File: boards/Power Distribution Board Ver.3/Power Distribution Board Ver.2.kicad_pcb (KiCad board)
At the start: 4 copper layers, 70 x 100 mm, 79 parts, among them J1 Screw_Terminal_01x02, J4 Screw_Terminal_01x06, U1 SIC431AED-T1-GE3, U2 SIC431AED-T1-GE3, U3 SIC431AED-T1-GE3

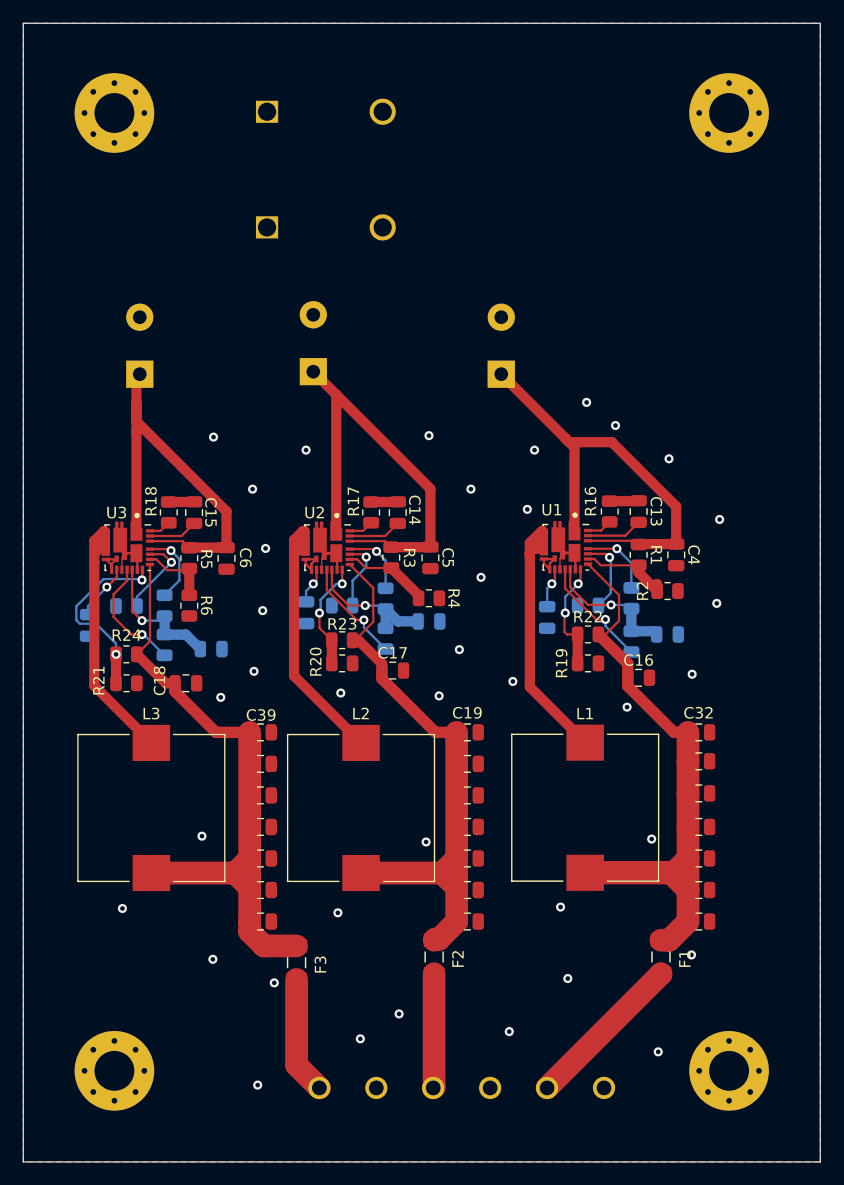
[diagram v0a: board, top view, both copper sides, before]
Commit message: GL connections and minor trace fixes
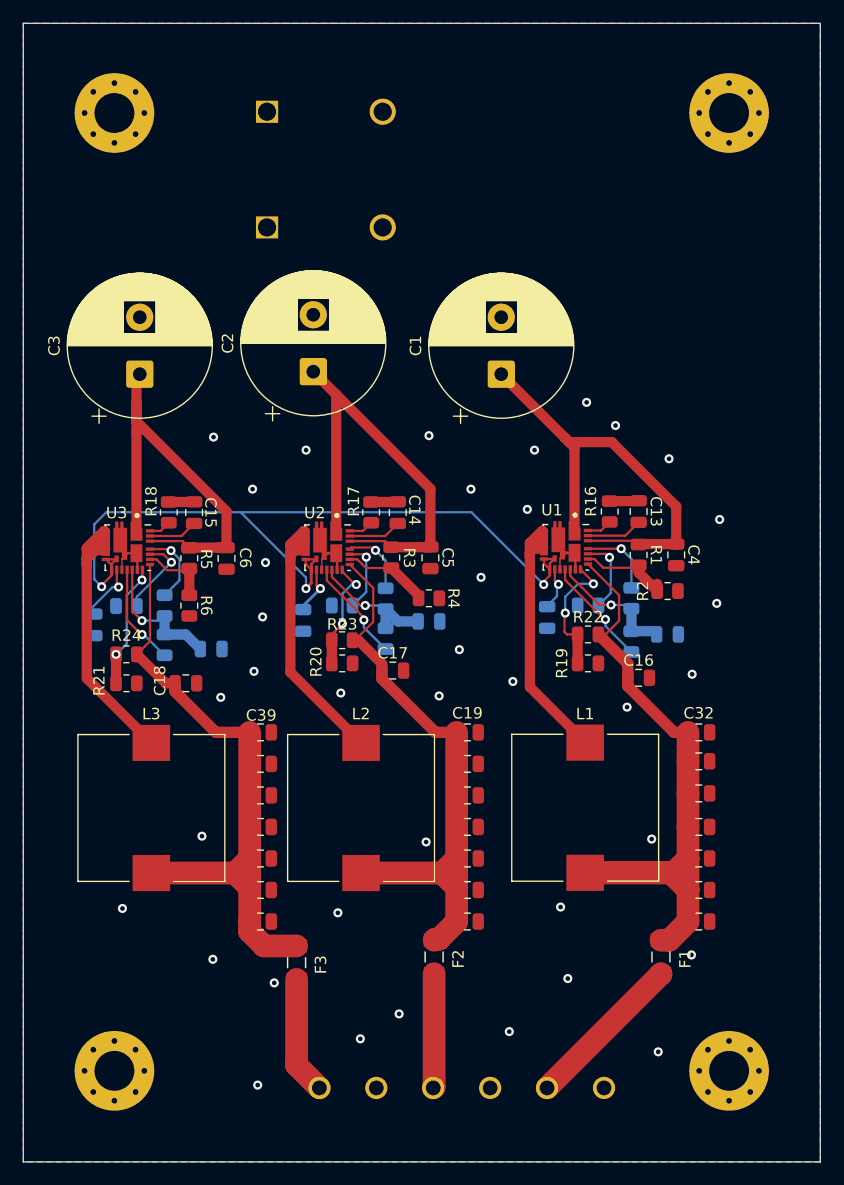
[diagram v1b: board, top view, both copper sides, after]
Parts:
- C1, C2, C3: moved to F.Cu
- L1, L2, L3: value 1uH -> 1.2uH
- R16, R17, R18: value 0 -> 3.3
- R22, R23: value 78.7k -> 73.2
- R24: value 78.7k -> 73.2k
- moved C11 0.72 mm to (42.6, 75.4)
- moved C12 0.55 mm to (24.2, 75.8)
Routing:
- net /GL: track 9.65 -> 72.3 mm, vias 0 -> 3
- net Net-(L3-Pad1): track 24.3 -> 31.8 mm
- net Net-(U3-FB): track 16.7 -> 11.0 mm
- net Net-(L2-Pad1): track 24.5 -> 29.8 mm
- net Net-(U1-FB): track 9.86 -> 11.6 mm
- net Net-(U3-PGOOD): track 10.5 -> 9.00 mm
- net Net-(U2-VDRV): track 3.21 -> 4.39 mm
- net Net-(U2-VDD): track 12.1 -> 11.5 mm
- net Net-(U1-VDD): track 12.0 -> 11.5 mm

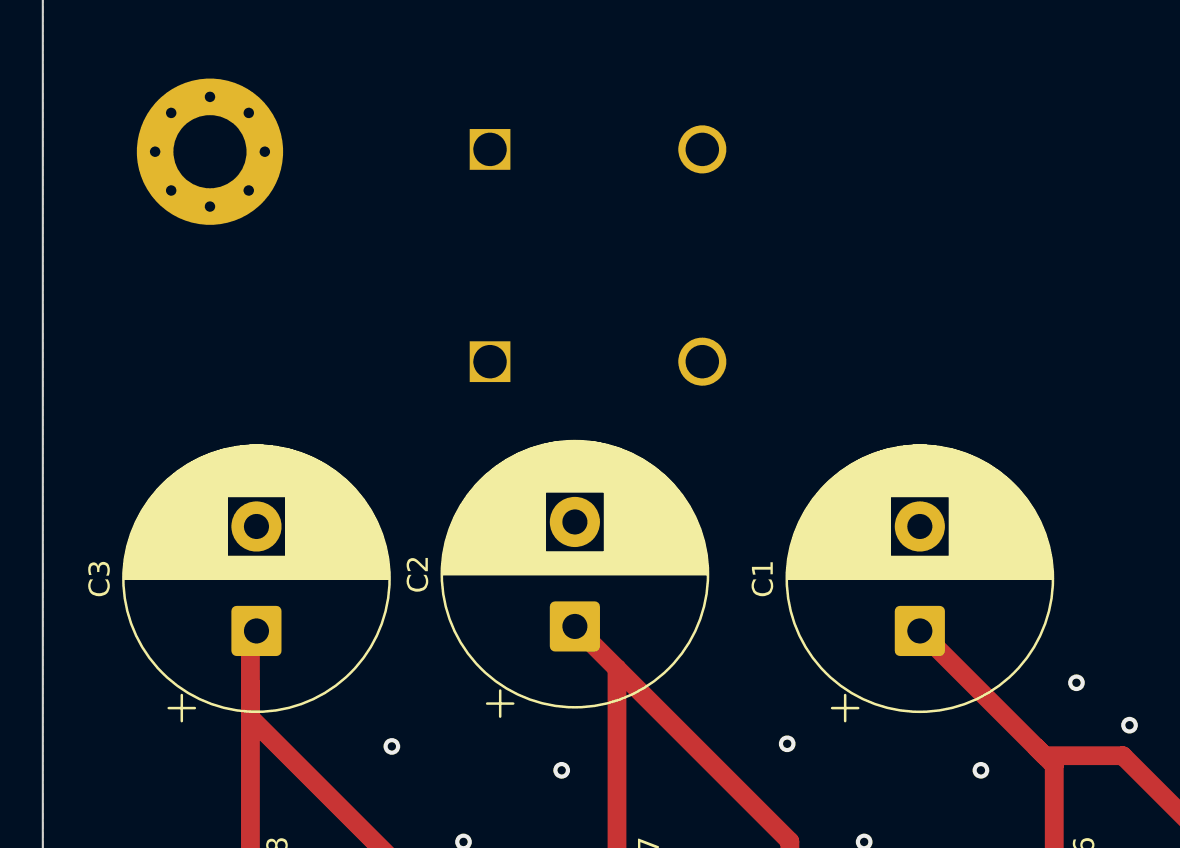
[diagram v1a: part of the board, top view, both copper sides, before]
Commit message: Fixed footprint warnings on caps and screw terminal
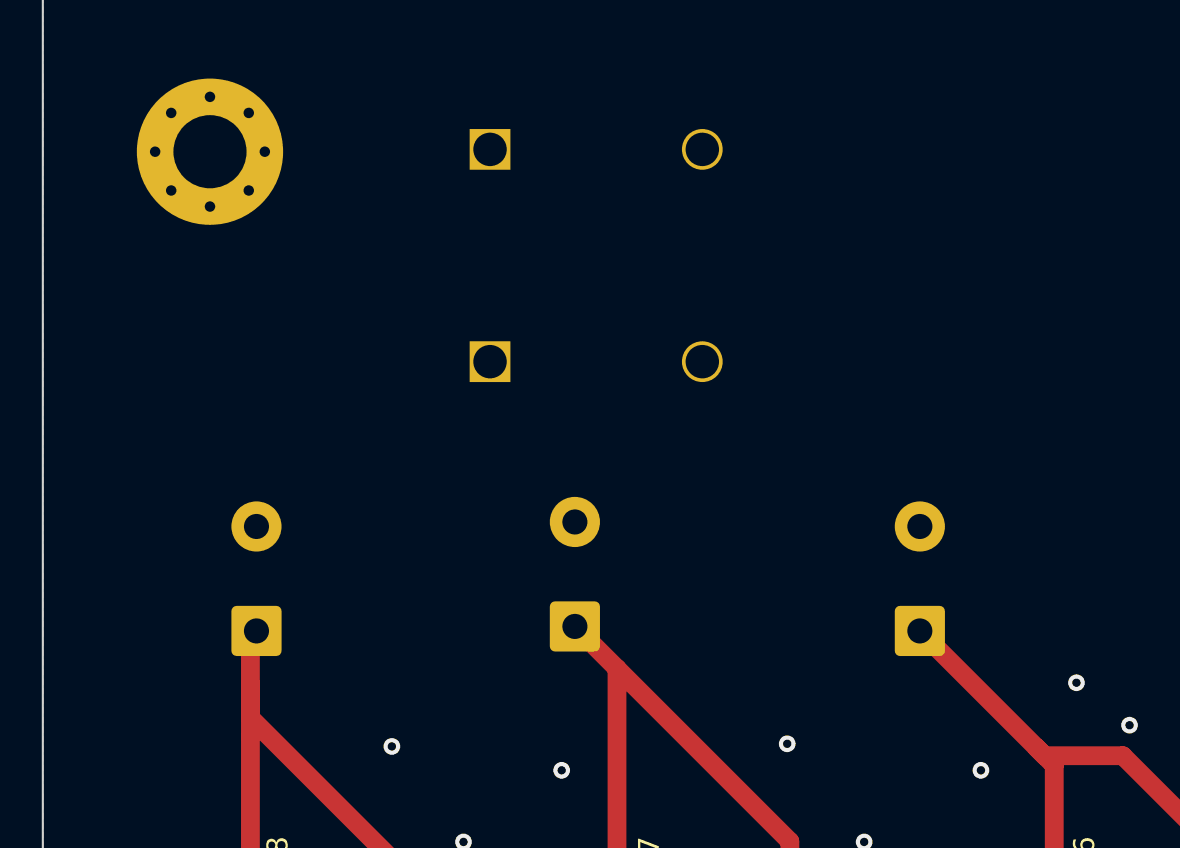
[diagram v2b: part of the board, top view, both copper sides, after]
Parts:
- C1, C2, C3: moved to B.Cu
